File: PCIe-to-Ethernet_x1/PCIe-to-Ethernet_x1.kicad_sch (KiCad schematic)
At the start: 68 parts, among them J1 1-406541-1, J2 Bus_PCI_Express_x1, T1 SM51625EL, Y1 WTL3M85411FO

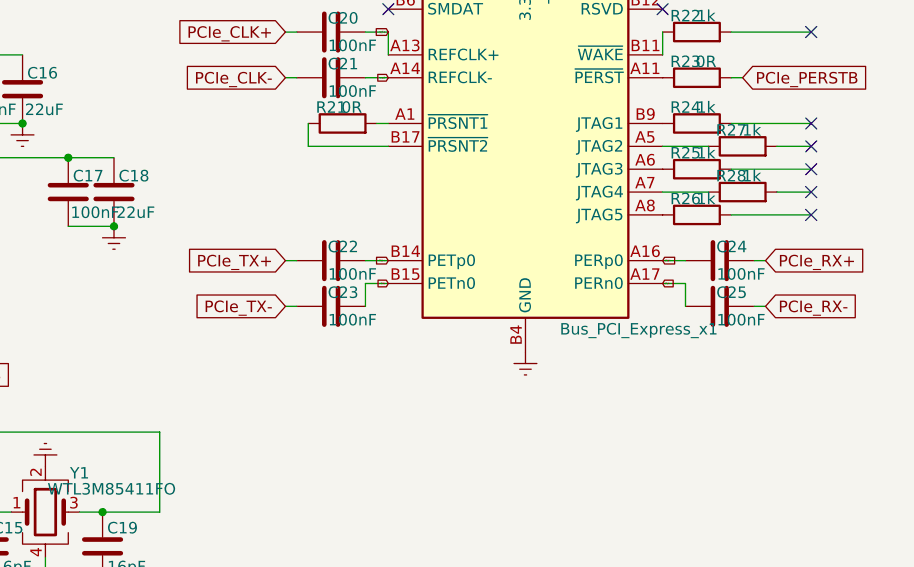
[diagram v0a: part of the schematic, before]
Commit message: Исправил отсутствие перекрёстного соединения на  PCIe
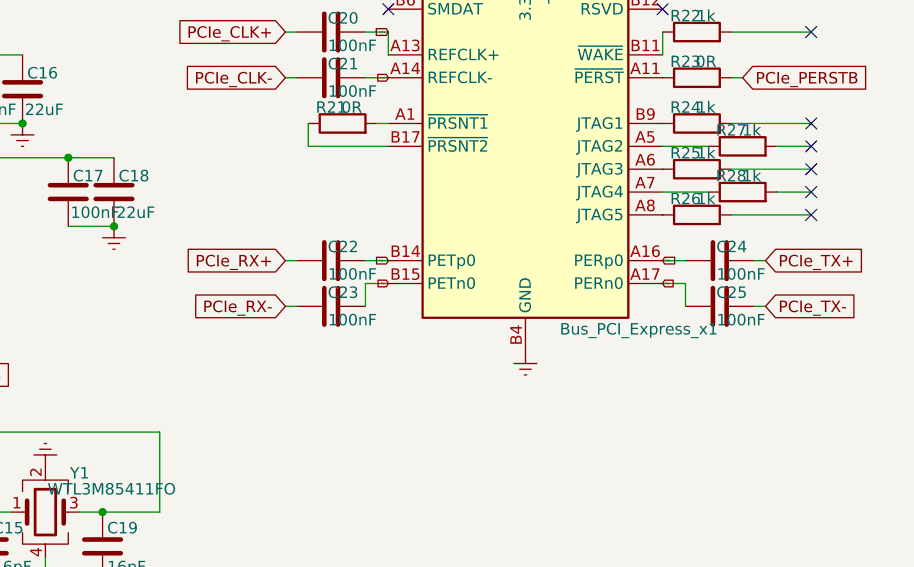
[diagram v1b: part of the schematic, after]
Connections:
- net PCIe_RX+: now also C22.1; no longer C24.2
- net PCIe_RX-: now also C23.1; no longer C25.2
- net PCIe_TX+: now also C24.2; no longer C22.1
- net PCIe_TX-: now also C25.2; no longer C23.1
